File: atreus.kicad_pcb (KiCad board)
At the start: 2 copper layers, 232 x 90 mm, 85 parts

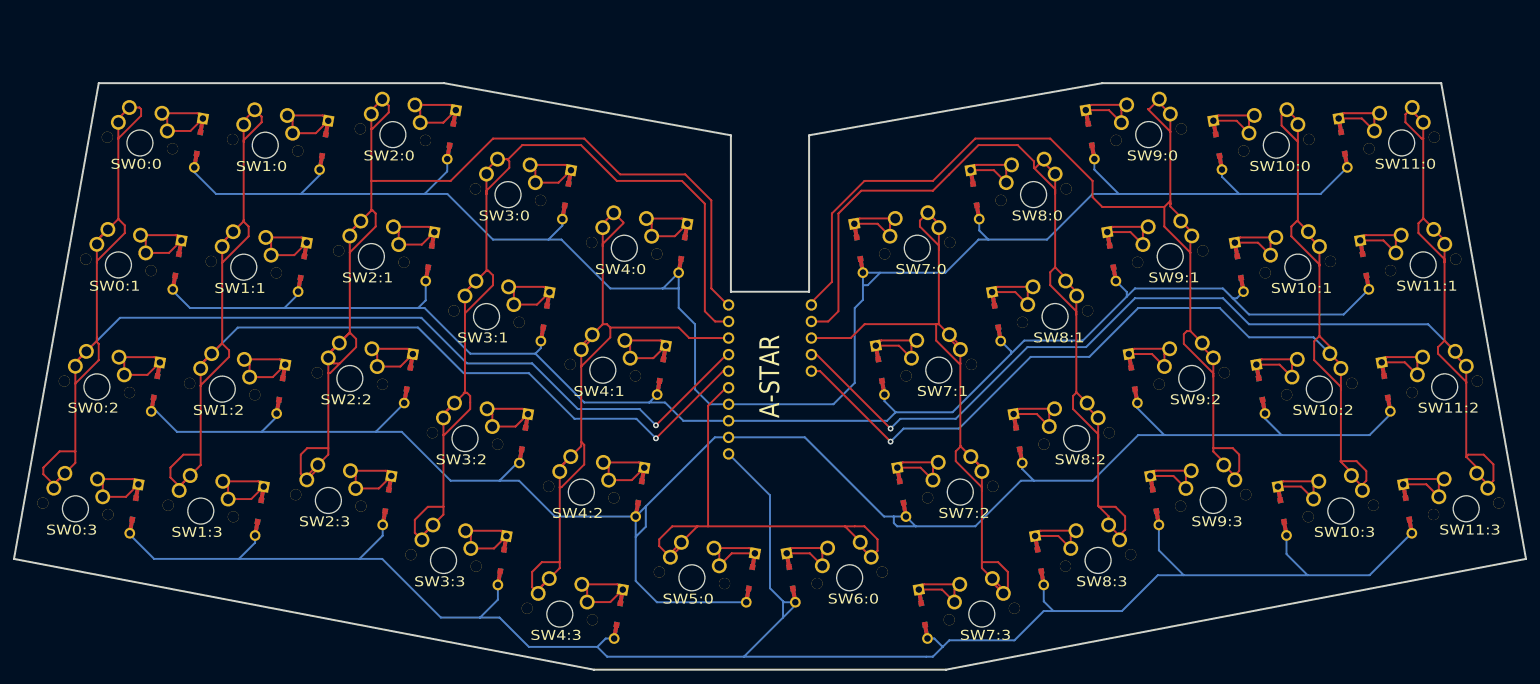
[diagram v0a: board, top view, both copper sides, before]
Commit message: Redesign PCB; rev 3.
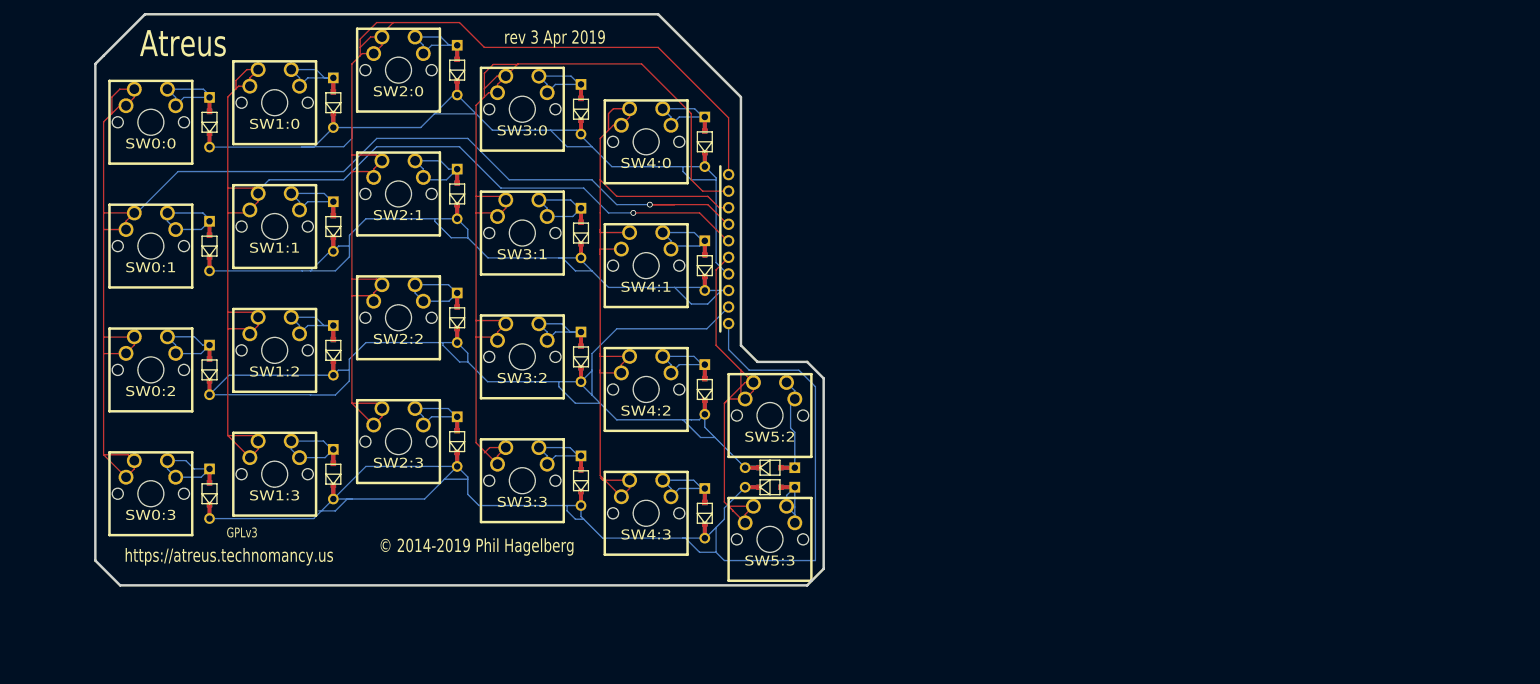
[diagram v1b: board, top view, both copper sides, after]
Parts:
- removed the D2:2 at (46.3, 31.2)
- removed the D2:2 at (81.8, 48.6)
- removed the D2:2 at (78.5, 67.3)
- removed the D2:2 at (75.2, 86.0)
- removed the D2:2 at (102.8, 39.1)
- removed the D2:2 at (99.5, 57.8)
- removed the D2:2 at (96.2, 76.5)
- removed the D2:2 at (92.9, 95.2)
- removed the D2:2 at (120.6, 47.3)
- removed the D2:2 at (117.3, 66.0)
- removed the D2:2 at (114.0, 84.8)
- removed the D2:2 at (43.0, 49.9)
- removed the D2:2 at (110.7, 103.5)
- removed the D2:2 at (131.0, 97.9)
- removed the D2:2 at (137.2, 97.9)
- removed the D2:2 at (147.6, 47.3)
- removed the D2:2 at (150.9, 66.0)
- removed the D2:2 at (154.2, 84.7)
- removed the D2:2 at (157.5, 103.5)
- removed the D2:2 at (165.4, 39.1)
- removed the D2:2 at (168.7, 57.8)
- removed the D2:2 at (172.0, 76.5)
- removed the D2:2 at (39.7, 68.6)
- removed the D2:2 at (175.3, 95.2)
- removed the D2:2 at (183.1, 29.9)
- removed the D2:2 at (186.4, 48.6)
- removed the D2:2 at (189.7, 67.3)
- removed the D2:2 at (193.0, 86.0)
- removed the D2:2 at (202.7, 31.5)
- removed the D2:2 at (206.0, 50.2)
- removed the D2:2 at (209.3, 68.9)
- removed the D2:2 at (212.6, 87.7)
- removed the D2:2 at (221.9, 31.2)
- removed the D2:2 at (36.4, 87.3)
- removed the D2:2 at (225.2, 49.9)
- removed the D2:2 at (228.5, 68.6)
- removed the D2:2 at (231.8, 87.3)
- removed the D2:2 at (65.6, 31.5)
- removed the D2:2 at (62.3, 50.2)
- removed the D2:2 at (59.0, 68.9)
- removed the D2:2 at (55.7, 87.7)
- removed the D2:2 at (85.1, 29.9)
- removed SW10:0, SW10:1, SW10:2, SW10:3, SW11:0, SW11:1, SW11:2, SW11:3, SW5:0, SW6:0, SW7:0, SW7:1, SW7:2, SW7:3, SW8:0, SW8:1, SW8:2, SW8:3, SW9:0, SW9:1, SW9:2, SW9:3: , MX_FLIP
- added D2:2: , DIODE, F.Cu at (48.0, 28.0)
- added D2:2: , DIODE, F.Cu at (86.0, 39.0)
- added D2:2: , DIODE, F.Cu at (86.0, 58.0)
- added D2:2: , DIODE, F.Cu at (86.0, 77.0)
- added D2:2: , DIODE, F.Cu at (105.0, 26.0)
- added D2:2: , DIODE, F.Cu at (105.0, 45.0)
- added D2:2: , DIODE, F.Cu at (105.0, 64.0)
- added D2:2: , DIODE, F.Cu at (105.0, 83.0)
- added D2:2: , DIODE, F.Cu at (124.0, 31.0)
- added D2:2: , DIODE, F.Cu at (124.0, 50.0)
- added D2:2: , DIODE, F.Cu at (124.0, 69.0)
- added D2:2: , DIODE, F.Cu at (48.0, 47.0)
- added D2:2: , DIODE, F.Cu at (124.0, 88.0)
- added D2:2: , DIODE, F.Cu at (134.0, 81.0)
- added D2:2: , DIODE, F.Cu at (134.0, 84.0)
- added D2:2: , DIODE, F.Cu at (48.0, 66.0)
- added D2:2: , DIODE, F.Cu at (48.0, 85.0)
- added D2:2: , DIODE, F.Cu at (67.0, 25.0)
- added D2:2: , DIODE, F.Cu at (67.0, 44.0)
- added D2:2: , DIODE, F.Cu at (67.0, 63.0)
- added D2:2: , DIODE, F.Cu at (67.0, 82.0)
- added D2:2: , DIODE, F.Cu at (86.0, 20.0)
- added SW5:2: , MX_FLIP, F.Cu at (134.0, 73.0)
- added SW5:3: , MX_FLIP, F.Cu at (134.0, 92.0)
- ?: value A-STAR -> (none)
- moved SW4:3 20.4 mm to (115.0, 88.0), turned to 0 degrees
- moved ? 20.0 mm to (134.0, 50.0)
- moved SW4:2 18.6 mm to (115.0, 69.0), turned to 0 degrees
- moved SW4:1 17.4 mm to (115.0, 50.0), turned to 0 degrees
- moved SW3:3 17.2 mm to (96.0, 83.0), turned to 0 degrees
- moved SW4:0 16.7 mm to (115.0, 31.0), turned to 0 degrees
- moved SW3:2 15.3 mm to (96.0, 64.0), turned to 0 degrees
- moved SW2:3 14.1 mm to (77.0, 77.0), turned to 0 degrees
- moved SW3:1 13.9 mm to (96.0, 45.0), turned to 0 degrees
- moved SW3:0 13.3 mm to (96.0, 26.0), turned to 0 degrees
- moved SW1:3 12.7 mm to (58.0, 82.0), turned to 0 degrees
- moved SW2:2 11.9 mm to (77.0, 58.0), turned to 0 degrees
- moved SW0:3 11.8 mm to (39.0, 85.0), turned to 0 degrees
- moved SW2:1 10.5 mm to (77.0, 39.0), turned to 0 degrees
- moved SW1:2 10.0 mm to (58.0, 63.0), turned to 0 degrees
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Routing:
- net N-col-10: track 211.5 -> 0.00 mm, vias 1 -> 0
- net N-col-9: track 193.0 -> 0.00 mm, vias 1 -> 0
- net N-col-8: track 176.2 -> 0.00 mm
- net N-col-7: track 153.6 -> 0.00 mm
- net N-row-0: track 264.8 -> 132.1 mm
- net N-col-6: track 124.5 -> 0.00 mm
- net N-row-2: track 281.8 -> 173.4 mm
- net N-row-1: track 226.9 -> 121.1 mm
- net N-row-3: track 299.5 -> 202.7 mm
- net N-diode-32: track 15.9 -> 0.00 mm
- net N-diode-25: track 15.9 -> 0.00 mm
- net N-diode-38: track 15.9 -> 0.00 mm
- net N-diode-33: track 15.9 -> 0.00 mm
- net N-diode-29: track 15.9 -> 0.00 mm
- net N-diode-26: track 15.9 -> 0.00 mm
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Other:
- board size 232 x 90 mm -> 111.8 x 87.6 mm
- board text added: "Atreus"
- board text added: "GPLv3"
- board text added: "https://atreus.technomancy.us"
- board text added: "rev 3 Apr 2019"
- board text added: "© 2014-2019 Phil Hagelberg"
